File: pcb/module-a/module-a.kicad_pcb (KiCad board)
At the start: 2 copper layers, 76 x 176 mm, 37 parts, among them J1 Conn_01x06, J2 Conn_01x06, SW1 SW_Push, SW10 SW_Push, SW11 SW_Push, SW12 SW_Push, SW2 SW_Push, SW3 SW_Push, SW4 SW_Push, SW5 SW_Push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

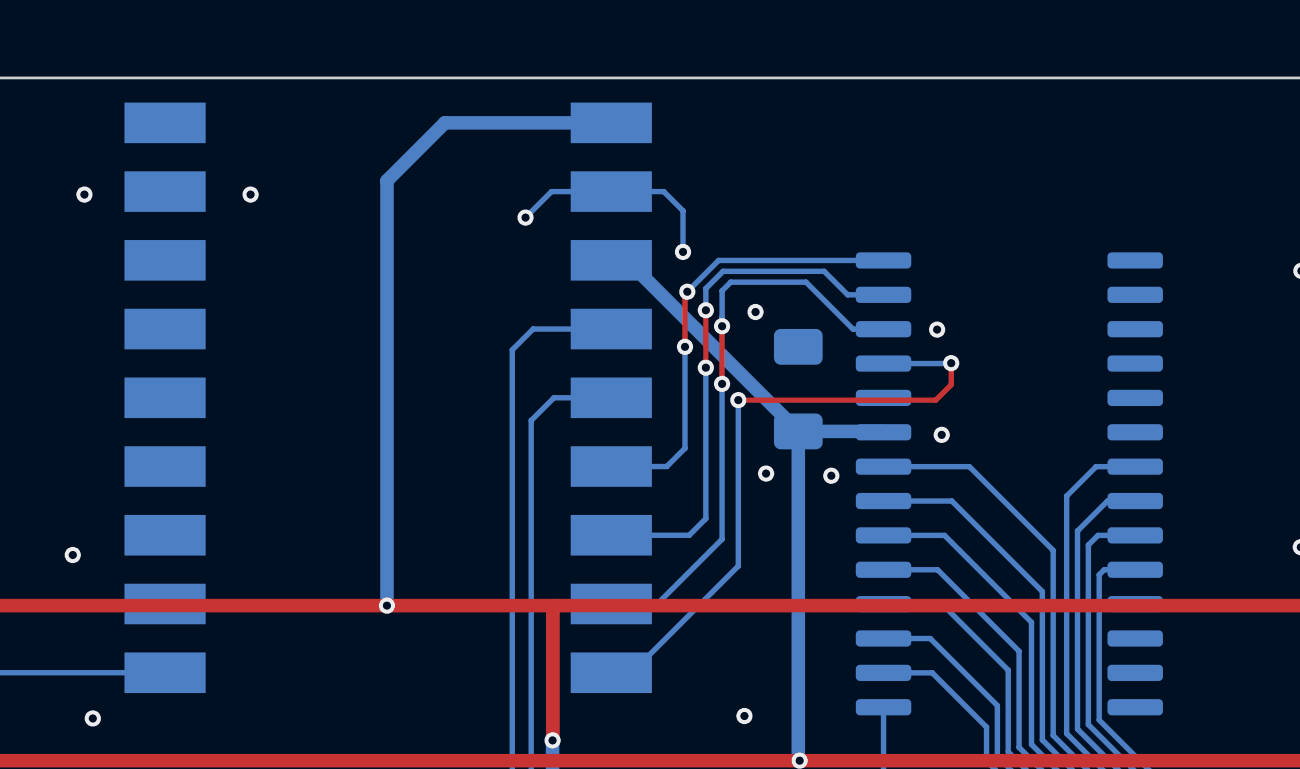
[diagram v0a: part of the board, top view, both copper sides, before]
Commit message: Extract modular firmware
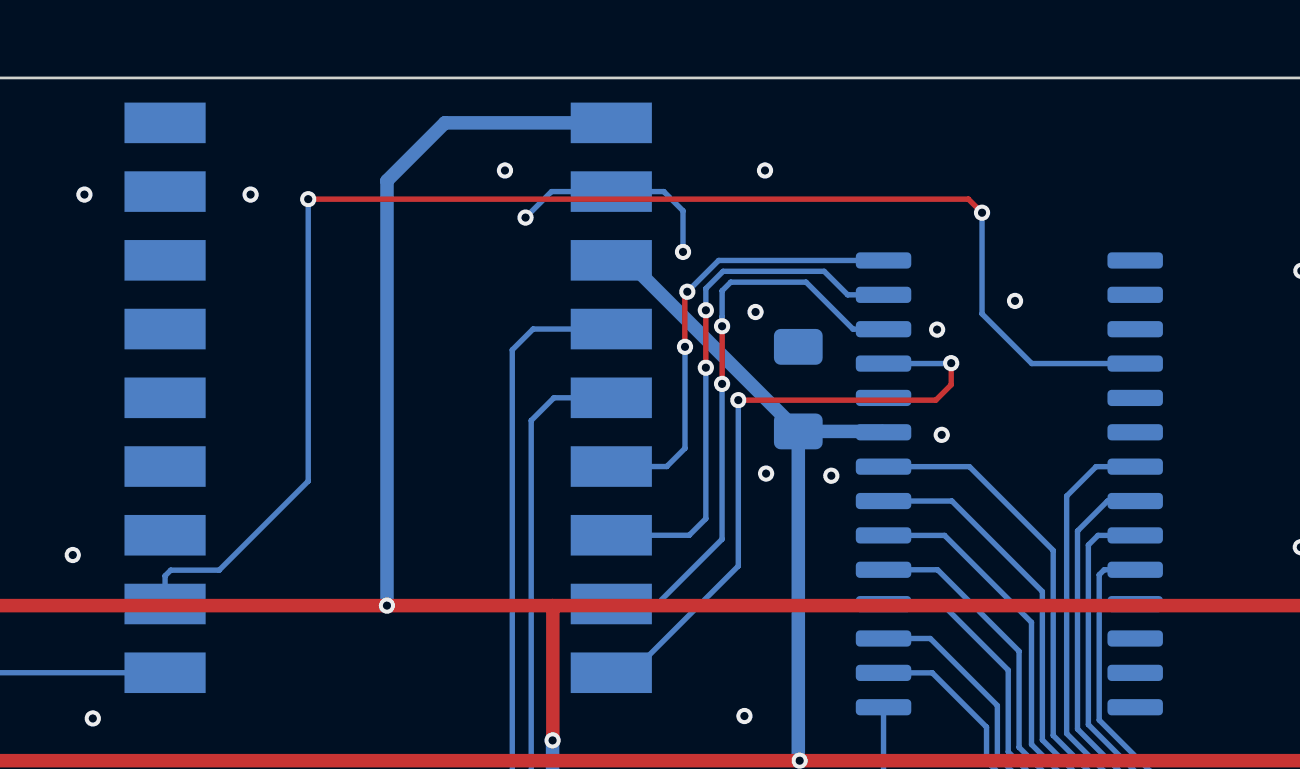
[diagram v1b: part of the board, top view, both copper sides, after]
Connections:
- U1 pad 11: unconnected-(U1-IO7-Pad11) -> Net-(U1-IO7)
- U2 pad 18: GND -> Net-(U1-IO7)
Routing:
- net Net-(U1-IO7): track 0.00 -> 53.5 mm, vias 0 -> 2
- net GND: vias 84 -> 87
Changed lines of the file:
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@@
 	(net 2 "Net-(U2-GPB0)")
 	(net 3 "unconnected-(U1-IO8-Pad12)")
-	(net 4 "unconnected-(U1-IO7-Pad11)")
+	(net 4 "Net-(U1-IO7)")
 	(net 5 "Net-(U2-GPB1)")
 	(net 6 "unconnected-(U1-IO18-Pad15)")
@@
 		(property ki_fp_filters "MountingHole*")
 		(sheetname "/")
-		(sheetfile "modular-key-pad.kicad_sch")
+		(sheetfile "module-a.kicad_sch")
 		(attr exclude_from_pos_files exclude_from_bom)
 		(fp_circle
@@
 		)
 		(sheetname "/")
-		(sheetfile "modular-key-pad.kicad_sch")
+		(sheetfile "module-a.kicad_sch")
 		(attr smd)
 		(fp_line
@@
 		(property ki_fp_filters "MountingHole*")
 		(sheetname "/")
-		(sheetfile "modular-key-pad.kicad_sch")
+		(sheetfile "module-a.kicad_sch")
 		(attr exclude_from_pos_files exclude_from_bom)
 		(fp_circle
@@
 		)
 		(sheetname "/")
-		(sheetfile "modular-key-pad.kicad_sch")
+		(sheetfile "module-a.kicad_sch")
 		(attr smd)
 		(fp_line
@@
 		(property ki_fp_filters "Connector*:*_1x??_*")
 		(sheetname "/")
-		(sheetfile "modular-key-pad.kicad_sch")
+		(sheetfile "module-a.kicad_sch")
 		(attr through_hole)
 		(fp_line
@@
 		)
 		(sheetname "/")
-		(sheetfile "modular-key-pad.kicad_sch")
+		(sheetfile "module-a.kicad_sch")
 		(attr smd)
 		(fp_line
@@
 		)
 		(sheetname "/")
-		(sheetfile "modular-key-pad.kicad_sch")
+		(sheetfile "module-a.kicad_sch")
 		(attr smd)
 		(fp_line
@@
 		)
 		(sheetname "/")
-		(sheetfile "modular-key-pad.kicad_sch")
+		(sheetfile "module-a.kicad_sch")
 		(attr smd)
 		(fp_line
@@
 		)
 		(sheetname "/")
-		(sheetfile "modular-key-pad.kicad_sch")
+		(sheetfile "module-a.kicad_sch")
 		(attr smd)
 		(fp_line
@@
 		)
 		(sheetname "/")
-		(sheetfile "modular-key-pad.kicad_sch")
+		(sheetfile "module-a.kicad_sch")
 		(attr smd)
 		(fp_line
@@
 		)
 		(sheetname "/")
-		(sheetfile "modular-key-pad.kicad_sch")
+		(sheetfile "module-a.kicad_sch")
 		(attr smd)
 		(fp_line
@@
 		(property ki_fp_filters "MountingHole*")
 		(sheetname "/")
-		(sheetfile "modular-key-pad.kicad_sch")
+		(sheetfile "module-a.kicad_sch")
 		(attr exclude_from_pos_files exclude_from_bom)
 		(fp_circle
@@
 		)
 		(sheetname "/")
-		(sheetfile "modular-key-pad.kicad_sch")
+		(sheetfile "module-a.kicad_sch")
 		(attr smd)
 		(fp_line
@@
 		)
 		(sheetname "/")
-		(sheetfile "modular-key-pad.kicad_sch")
+		(sheetfile "module-a.kicad_sch")
 		(attr smd)
 		(fp_line
@@
 		(property ki_fp_filters "MountingHole*")
 		(sheetname "/")
-		(sheetfile "modular-key-pad.kicad_sch")
+		(sheetfile "module-a.kicad_sch")
 		(attr exclude_from_pos_files exclude_from_bom)
 		(fp_circle
@@
 		(property ki_fp_filters "MountingHole*")
 		(sheetname "/")
-		(sheetfile "modular-key-pad.kicad_sch")
+		(sheetfile "module-a.kicad_sch")
 		(attr exclude_from_pos_files exclude_from_bom)
 		(fp_circle
@@
 		(property ki_fp_filters "Connector*:*_1x??_*")
 		(sheetname "/")
-		(sheetfile "modular-key-pad.kicad_sch")
+		(sheetfile "module-a.kicad_sch")
 		(attr through_hole)
 		(fp_line
@@
 		)
 		(sheetname "/")
-		(sheetfile "modular-key-pad.kicad_sch")
+		(sheetfile "module-a.kicad_sch")
 		(attr smd)
 		(fp_line
@@
 		)
 		(sheetname "/")
-		(sheetfile "modular-key-pad.kicad_sch")
+		(sheetfile "module-a.kicad_sch")
 		(attr smd)
 		(fp_line
@@
 		(property ki_fp_filters "MountingHole*")
 		(sheetname "/")
-		(sheetfile "modular-key-pad.kicad_sch")
+		(sheetfile "module-a.kicad_sch")
 		(attr exclude_from_pos_files exclude_from_bom)
 		(fp_circle
@@
 		(property ki_fp_filters "DIP?20* SOIC*7.5x12.8mm*P1.27mm* TSSOP*4.4x6.5mm*P0.65mm* SSOP*4.4x6.5mm*P0.65mm*")
 		(sheetname "/")
-		(sheetfile "modular-key-pad.kicad_sch")
+		(sheetfile "module-a.kicad_sch")
 		(attr smd)
 		(fp_line
@@
 		)
 		(sheetname "/")
-		(sheetfile "modular-key-pad.kicad_sch")
+		(sheetfile "module-a.kicad_sch")
 		(attr smd)
 		(fp_poly
@@
 		)
 		(sheetname "/")
-		(sheetfile "modular-key-pad.kicad_sch")
+		(sheetfile "module-a.kicad_sch")
 		(attr smd)
 		(fp_poly
@@
 		)
 		(sheetname "/")
-		(sheetfile "modular-key-pad.kicad_sch")
+		(sheetfile "module-a.kicad_sch")
 		(attr smd)
 		(fp_poly
@@
 		)
 		(sheetname "/")
-		(sheetfile "modular-key-pad.kicad_sch")
+		(sheetfile "module-a.kicad_sch")
 		(attr smd)
 		(fp_poly
@@
 		)
 		(sheetname "/")
-		(sheetfile "modular-key-pad.kicad_sch")
+		(sheetfile "module-a.kicad_sch")
 		(attr smd)
 		(fp_poly
@@
 		(property ki_fp_filters "C_*")
 		(sheetname "/")
-		(sheetfile "modular-key-pad.kicad_sch")
+		(sheetfile "module-a.kicad_sch")
 		(attr smd)
 		(fp_line
@@
 		(property ki_fp_filters "SOIC*7.5x17.9mm*P1.27mm*")
 		(sheetname "/")
-		(sheetfile "modular-key-pad.kicad_sch")
+		(sheetfile "module-a.kicad_sch")
 		(attr smd)
 		(fp_line
@@
 			(layers "B.Cu" "B.Mask" "B.Paste")
 			(roundrect_rratio 0.25)
-			(net 37 "GND")
+			(net 4 "Net-(U1-IO7)")
 			(pinfunction "~{RESET}")
 			(pintype "input")
@@
 		)
 		(sheetname "/")
-		(sheetfile "modular-key-pad.kicad_sch")
+		(sheetfile "module-a.kicad_sch")
 		(attr smd)
 		(fp_poly
@@
 		)
 		(sheetname "/")
-		(sheetfile "modular-key-pad.kicad_sch")
+		(sheetfile "module-a.kicad_sch")
 		(attr smd)
 		(fp_poly
@@
 		)
 		(sheetname "/")
-		(sheetfile "modular-key-pad.kicad_sch")
+		(sheetfile "module-a.kicad_sch")
 		(attr smd)
 		(fp_poly
@@
 		)
 		(sheetname "/")
-		(sheetfile "modular-key-pad.kicad_sch")
+		(sheetfile "module-a.kicad_sch")
 		(attr smd)
 		(fp_poly
@@
 		)
 		(sheetname "/")
-		(sheetfile "modular-key-pad.kicad_sch")
+		(sheetfile "module-a.kicad_sch")
 		(attr smd)
 		(fp_rect
@@
 			(size 3 1.5)
 			(layers "B.Cu" "B.Mask" "B.Paste")
-			(net 4 "unconnected-(U1-IO7-Pad11)")
+			(net 4 "Net-(U1-IO7)")
 			(pinfunction "IO7")
-			(pintype "bidirectional+no_connect")
+			(pintype "bidirectional")
 			(thermal_bridge_angle 45)
 		)
@@
 		)
 		(sheetname "/")
-		(sheetfile "modular-key-pad.kicad_sch")
+		(sheetfile "module-a.kicad_sch")
 		(attr smd)
 		(fp_poly
@@
 		)
 		(sheetname "/")
-		(sheetfile "modular-key-pad.kicad_sch")
+		(sheetfile "module-a.kicad_sch")
 		(attr smd)
 		(fp_poly
@@
 		)
 		(sheetname "/")
-		(sheetfile "modular-key-pad.kicad_sch")
+		(sheetfile "module-a.kicad_sch")
 		(attr smd)
 		(fp_poly
@@
 		(property ki_fp_filters "C_*")
 		(sheetname "/")
-		(sheetfile "modular-key-pad.kicad_sch")
+		(sheetfile "module-a.kicad_sch")
 		(attr smd)
 		(fp_line
@@
 	)
 	(segment
+		(start 151.2525 25.524)
+		(end 126.8525 25.524)
+		(width 0.2)
+		(layer "F.Cu")
+		(net 4)
+	)
+	(segment
+		(start 151.7525 26.024)
+		(end 151.2525 25.524)
+		(width 0.2)
+		(layer "F.Cu")
+		(net 4)
+	)
+	(via
+		(at 126.8525 25.524)
+		(size 0.6)
+		(drill 0.3)
+		(layers "F.Cu" "B.Cu")
+		(net 4)
+	)
+	(via
+		(at 151.7525 26.024)
+		(size 0.6)
+		(drill 0.3)
+		(layers "F.Cu" "B.Cu")
+		(net 4)
+	)
+	(segment
+		(start 121.7725 39.234)
+		(end 121.5625 39.444)
+		(width 0.2)
+		(layer "B.Cu")
+		(net 4)
+	)
+	(segment
+		(start 157.4125 31.599)
+		(end 153.589468 31.599)
+		(width 0.2)
+		(layer "B.Cu")
+		(net 4)
+	)
+	(segment
+		(start 151.7525 29.762032)
+		(end 151.7525 26.024)
+		(width 0.2)
+		(layer "B.Cu")
+		(net 4)
+	)
+	(segment
+		(start 153.589468 31.599)
+		(end 151.7525 29.762032)
+		(width 0.2)
+		(layer "B.Cu")
+		(net 4)
+	)
+	(segment
+		(start 121.5625 39.444)
+		(end 121.5625 40.484)
+		(width 0.2)
+		(layer "B.Cu")
+		(net 4)
+	)
+	(segment
+		(start 123.5625 39.234)
+		(end 121.7725 39.234)
+		(width 0.2)
+		(layer "B.Cu")
+		(net 4)
+	)
+	(segment
+		(start 126.8525 25.524)
+		(end 126.8525 35.944)
+		(width 0.2)
+		(layer "B.Cu")
+		(net 4)
+	)
+	(segment
+		(start 126.8525 35.944)
+		(end 123.5625 39.234)
+		(width 0.2)
+		(layer "B.Cu")
+		(net 4)
+	)
+	(segment
 		(start 151.9185 45.034)
 		(end 149.9135 43.029)
@@
 	)
 	(via
+		(at 152.9725 29.284)
+		(size 0.6)
+		(drill 0.3)
+		(layers "F.Cu" "B.Cu")
+		(free yes)
+		(net 37)
+	)
+	(via
 		(at 143.1725 52.694)
 		(size 0.6)
@@
 	)
 	(via
+		(at 143.7325 24.464)
+		(size 0.6)
+		(drill 0.3)
+		(layers "F.Cu" "B.Cu")
+		(free yes)
+		(net 37)
+	)
+	(via
 		(at 142.3925 183.024)
 		(size 0.6)
@@
 		(size 0.6)
 		(drill 0.3)
+		(layers "F.Cu" "B.Cu")
+		(free yes)
+		(net 37)
+	)
+	(via
+		(at 134.1225 24.464)
+		(size 0.6)
+		(drill 0.3)

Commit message: Add module-b (rotary encoders x3)
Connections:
- net /~{CS} renamed /~{MCP_CS}
- net Net-(U1-IO7) renamed /~{MCP_RST}
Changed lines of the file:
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@@
 	(net 2 "Net-(U2-GPB0)")
 	(net 3 "unconnected-(U1-IO8-Pad12)")
-	(net 4 "Net-(U1-IO7)")
+	(net 4 "/~{MCP_RST}")
 	(net 5 "Net-(U2-GPB1)")
 	(net 6 "unconnected-(U1-IO18-Pad15)")
@@
 	(net 22 "Net-(U2-GPA3)")
 	(net 23 "/MISO")
-	(net 24 "/~{CS}")
+	(net 24 "/~{MCP_CS}")
 	(net 25 "/MOSI")
 	(net 26 "/SCK")
@@
 			(layers "B.Cu" "B.Mask" "B.Paste")
 			(roundrect_rratio 0.25)
-			(net 24 "/~{CS}")
+			(net 24 "/~{MCP_CS}")
 			(pinfunction "~{CS}")
 			(pintype "input")
@@
 			(layers "B.Cu" "B.Mask" "B.Paste")
 			(roundrect_rratio 0.25)
-			(net 4 "Net-(U1-IO7)")
+			(net 4 "/~{MCP_RST}")
 			(pinfunction "~{RESET}")
 			(pintype "input")
@@
 			(size 3 1.5)
 			(layers "B.Cu" "B.Mask" "B.Paste")
-			(net 24 "/~{CS}")
+			(net 24 "/~{MCP_CS}")
 			(pinfunction "IO5")
 			(pintype "bidirectional")
@@
 			(size 3 1.5)
 			(layers "B.Cu" "B.Mask" "B.Paste")
-			(net 4 "Net-(U1-IO7)")
+			(net 4 "/~{MCP_RST}")
 			(pinfunction "IO7")
 			(pintype "bidirectional")

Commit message: 3V net should not be shared across the bus
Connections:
- C1 pad 1: 3V3 -> Net-(U1-V3V)
- J1 pad 3: 3V3 -> Net-(J1-Pin_3)
- J2 pad 3: 3V3 -> Net-(J1-Pin_3)
- U1 pad 3: 3V3 -> Net-(U1-V3V)
- U2 pad 9: 3V3 -> Net-(U1-V3V)
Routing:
- net 3V3: track 94.0 -> 0.00 mm, vias 1 -> 0
- net Net-(J1-Pin_3): track 0.00 -> 69.2 mm
- net Net-(U1-V3V): track 0.00 -> 12.7 mm
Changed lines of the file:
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@@
 	(net 37 "GND")
 	(net 38 "5V")
-	(net 39 "3V3")
+	(net 39 "Net-(U1-V3V)")
 	(net 40 "/SLC")
 	(net 41 "/SDA")
@@
 	(net 56 "Net-(LED6-DIN)")
 	(net 57 "Net-(LED11-DIN)")
+	(net 58 "Net-(J1-Pin_3)")
 	(footprint "MountingHole:MountingHole_2.2mm_M2"
 		(layer "F.Cu")
@@
 			(layers "*.Cu" "*.Mask")
 			(remove_unused_layers no)
-			(net 39 "3V3")
+			(net 58 "Net-(J1-Pin_3)")
 			(pinfunction "Pin_3")
 			(pintype "passive")
@@
 			(layers "*.Cu" "*.Mask")
 			(remove_unused_layers no)
-			(net 39 "3V3")
+			(net 58 "Net-(J1-Pin_3)")
 			(pinfunction "Pin_3")
 			(pintype "passive")
@@
 			(layers "B.Cu" "B.Mask" "B.Paste")
 			(roundrect_rratio 0.188679)
-			(net 39 "3V3")
+			(net 39 "Net-(U1-V3V)")
 			(pintype "passive")
 		)
@@
 			(layers "B.Cu" "B.Mask" "B.Paste")
 			(roundrect_rratio 0.25)
-			(net 39 "3V3")
+			(net 39 "Net-(U1-V3V)")
 			(pinfunction "VDD")
 			(pintype "power_in")
@@
 			(size 3 1.5)
 			(layers "B.Cu" "B.Mask" "B.Paste")
-			(net 39 "3V3")
+			(net 39 "Net-(U1-V3V)")
 			(pinfunction "V3V")
 			(pintype "power_out")
@@
 	)
 	(segment
-		(start 145.0125 46.274)
-		(end 174.3225 46.274)
-		(width 0.5)
-		(layer "F.Cu")
-		(net 39)
-	)
-	(segment
-		(start 105.1875 46.274)
-		(end 145.0125 46.274)
-		(width 0.5)
-		(layer "F.Cu")
-		(net 39)
-	)
-	(segment
-		(start 174.3225 46.274)
-		(end 174.3325 46.264)
-		(width 0.5)
-		(layer "F.Cu")
-		(net 39)
-	)
-	(via
-		(at 145.0125 46.274)
-		(size 0.6)
-		(drill 0.3)
-		(layers "F.Cu" "B.Cu")
-		(net 39)
-	)
-	(segment
 		(start 144.9625 34.1065)
 		(end 148.08 34.1065)
@@
 	)
 	(segment
-		(start 144.9625 46.224)
-		(end 144.9625 34.1065)
-		(width 0.5)
-		(layer "B.Cu")
-		(net 39)
-	)
-	(segment
 		(start 138.64 27.784)
 		(end 138.0525 27.784)
@@
 	)
 	(segment
-		(start 145.0125 46.274)
-		(end 144.9625 46.224)
-		(width 0.5)
-		(layer "B.Cu")
-		(net 39)
-	)
-	(segment
 		(start 148.08 34.1065)
 		(end 148.1125 34.139)
@@
 		(net 57)
 	)
+	(segment
+		(start 105.1875 46.274)
+		(end 143.8825 46.274)
+		(width 0.2)
+		(layer "F.Cu")
+		(net 58)
+	)
+	(segment
+		(start 143.8925 46.264)
+		(end 174.3325 46.264)
+		(width 0.2)
+		(layer "F.Cu")
+		(net 58)
+	)
+	(segment
+		(start 174.3225 46.274)
+		(end 174.3325 46.264)
+		(width 0.5)
+		(layer "F.Cu")
+		(net 58)
+	)
+	(segment
+		(start 143.8825 46.274)
+		(end 143.8925 46.264)
+		(width 0.2)
+		(layer "F.Cu")
+		(net 58)
+	)
 	(zone
